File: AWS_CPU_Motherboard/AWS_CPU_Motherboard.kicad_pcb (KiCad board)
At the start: 4 copper layers, 255 x 305 mm, 53 parts, among them J1 Power, J10 UART B, J12 Video, J14 HDD Power, J15 HDD Power, J2 Speaker, J3 Cluster, J4 Cluster, J5 HDD Power, J6 Drive Type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

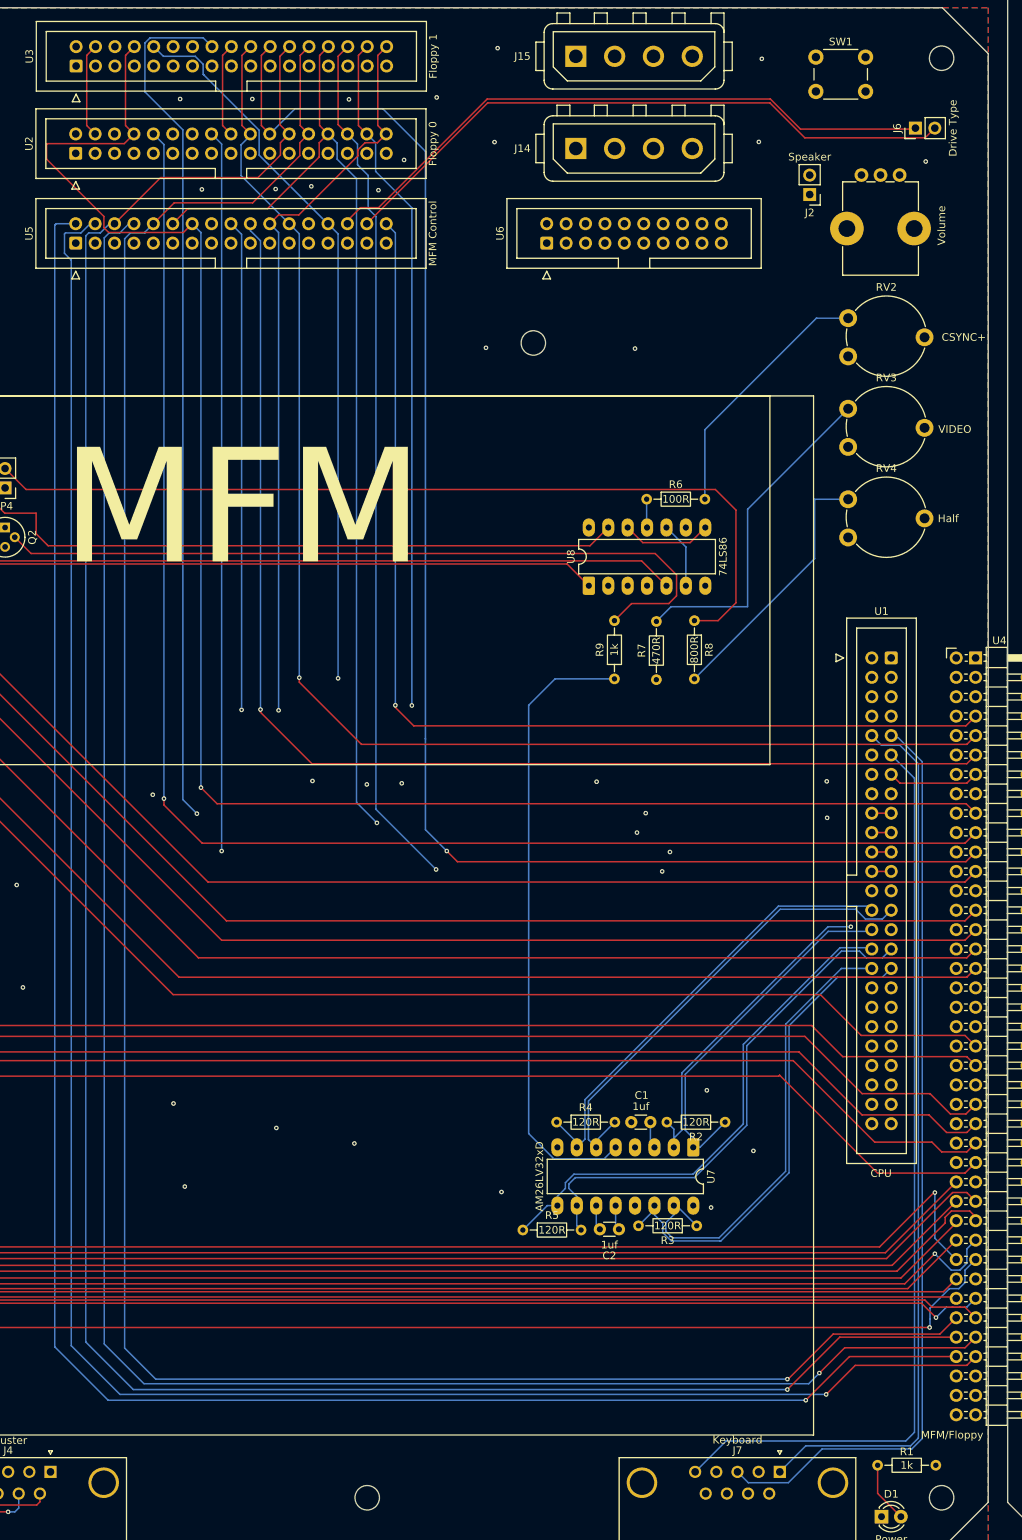
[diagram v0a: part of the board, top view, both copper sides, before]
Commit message: Update PCB to fix floppy drive & update video software to capure all the screen
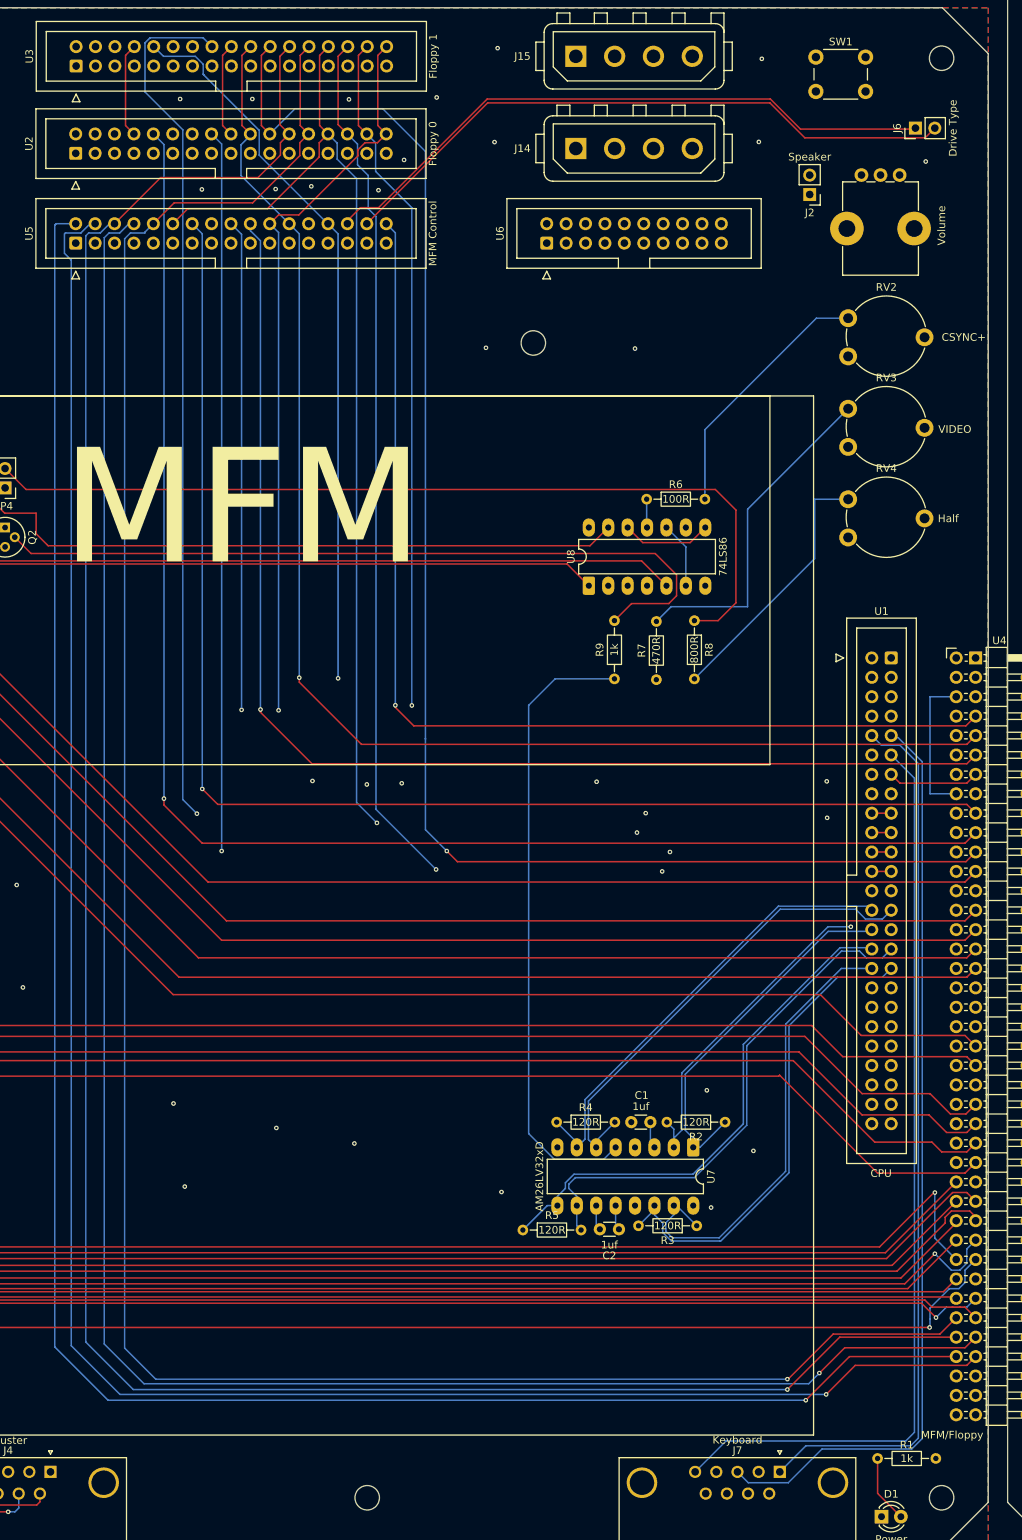
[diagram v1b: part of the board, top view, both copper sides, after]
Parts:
- moved R1 0.89 mm to (445.3, 450.2)
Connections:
- U2 pad 4: SIDED- -> unconnected-(U2-SIDED--Pad4)
- U2 pad 8: HDSEL0- -> INDEX-
- U3 pad 4: SIDED- -> unconnected-(U3-SIDED--Pad4)
- U3 pad 8: HDSEL0- -> INDEX-
- U4 pad 16: SIDED- -> 2SIDED-
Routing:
- net SIDED-: track 208.1 -> 0.00 mm, vias 1 -> 0
- net HDSEL0-: track 227.7 -> 177.1 mm
- net INDEX-: track 161.4 -> 196.0 mm
- net 2SIDED-: track 161.3 -> 180.9 mm
- net Net-(D1-A): track 7.99 -> 8.88 mm
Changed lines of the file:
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@@
 	(net 33 "WRDATA-")
 	(net 34 "RDDATA-")
-	(net 35 "SIDED-")
+	(net 35 "unconnected-(U2-SIDED--Pad4)")
 	(net 36 "WRGATE-")
 	(net 37 "unconnected-(U2-Pad12)")
@@
 	(net 173 "Net-(U8-Pad12)")
 	(net 174 "Net-(U8-Pad3)")
+	(net 175 "unconnected-(U3-SIDED--Pad4)")
 	(footprint "Connector_PinHeader_2.54mm:PinHeader_1x02_P2.54mm_Vertical"
 		(layer "F.Cu")
@@
 			(layers "*.Cu" "*.Mask")
 			(remove_unused_layers no)
-			(net 35 "SIDED-")
+			(net 32 "2SIDED-")
 			(pinfunction "SIDED-")
 			(pintype "bidirectional")
@@
 			(layers "*.Cu" "*.Mask")
 			(remove_unused_layers no)
-			(net 35 "SIDED-")
+			(net 175 "unconnected-(U3-SIDED--Pad4)")
 			(pinfunction "SIDED-")
-			(pintype "input")
+			(pintype "input+no_connect")
 		)
 		(pad "5" thru_hole circle
@@
 			(layers "*.Cu" "*.Mask")
 			(remove_unused_layers no)
-			(net 43 "HDSEL0-")
+			(net 71 "INDEX-")
 			(pinfunction "HDSEL0-")
 			(pintype "input")
@@
 			(layers "*.Cu" "*.Mask")
 			(remove_unused_layers no)
-			(net 35 "SIDED-")
+			(net 35 "unconnected-(U2-SIDED--Pad4)")
 			(pinfunction "SIDED-")
-			(pintype "input")
+			(pintype "input+no_connect")
 		)
 		(pad "5" thru_hole circle
@@
 			(layers "*.Cu" "*.Mask")
 			(remove_unused_layers no)
-			(net 43 "HDSEL0-")
+			(net 71 "INDEX-")
 			(pinfunction "HDSEL0-")
 			(pintype "input")
@@
 	(footprint "Resistor_THT:R_Axial_DIN0204_L3.6mm_D1.6mm_P7.62mm_Horizontal"
 		(layer "F.Cu")
-		(at 445.262 451.104 180)
+		(at 445.262 450.215 180)
 		(descr "Resistor, Axial_DIN0204 series, Axial, Horizontal, pin pitch=7.62mm, 0.167W, length*diameter=3.6*1.6mm^2, http://cdn-reichelt.de/documents/datenblatt/B400/1_4W%23YAG.pdf")
 		(tags "Resistor Axial_DIN0204 series Axial Horizontal pin pitch 7.62mm 0.167W length 3.6mm diameter 1.6mm")
@@
 	)
 	(segment
-		(start 437.642 451.104)
+		(start 437.642 450.215)
 		(end 437.642 454.787)
 		(width 0.2)
@@
 	)
 	(segment
+		(start 444.5 363.22)
+		(end 444.5 350.52)
+		(width 0.2)
+		(layer "B.Cu")
+		(net 32)
+	)
+	(segment
 		(start 371.9402 281.7702)
 		(end 371.9402 278.011)
@@
 	)
 	(segment
+		(start 444.5 350.52)
+		(end 447.929 350.52)
+		(width 0.2)
+		(layer "B.Cu")
+		(net 32)
+	)
+	(segment
+		(start 447.929 363.22)
+		(end 444.5 363.22)
+		(width 0.2)
+		(layer "B.Cu")
+		(net 32)
+	)
+	(segment
 		(start 387.85 351.671)
 		(end 446.778 351.671)
@@
 	)
 	(segment
-		(start 334.129 266.581)
-		(end 334.129 275.7598)
-		(width 0.2)
-		(layer "F.Cu")
-		(net 35)
-	)
-	(segment
-		(start 335.28 265.43)
-		(end 334.129 266.581)
-		(width 0.2)
-		(layer "F.Cu")
-		(net 35)
-	)
-	(segment
-		(start 334.129 275.7598)
-		(end 335.2292 276.86)
-		(width 0.2)
-		(layer "F.Cu")
-		(net 35)
-	)
-	(via
-		(at 342.773 363.347)
-		(size 0.6)
-		(drill 0.3)
-		(layers "F.Cu" "B.Cu")
-		(net 35)
-	)
-	(segment
-		(start 343.916 364.49)
-		(end 446.659 364.49)
-		(width 0.2)
-		(layer "In1.Cu")
-		(net 35)
-	)
-	(segment
-		(start 342.773 363.347)
-		(end 343.916 364.49)
-		(width 0.2)
-		(layer "In1.Cu")
-		(net 35)
-	)
-	(segment
-		(start 446.659 364.49)
-		(end 447.929 363.22)
-		(width 0.2)
-		(layer "In1.Cu")
-		(net 35)
-	)
-	(segment
-		(start 336.423 280.416)
-		(end 336.423 278.0538)
-		(width 0.2)
-		(layer "In2.Cu")
-		(net 35)
-	)
-	(segment
-		(start 336.423 278.0538)
-		(end 335.2292 276.86)
-		(width 0.2)
-		(layer "In2.Cu")
-		(net 35)
-	)
-	(segment
-		(start 341.63 362.204)
-		(end 341.63 285.623)
-		(width 0.2)
-		(layer "In2.Cu")
-		(net 35)
-	)
-	(segment
-		(start 341.63 285.623)
-		(end 336.423 280.416)
-		(width 0.2)
-		(layer "In2.Cu")
-		(net 35)
-	)
-	(segment
-		(start 342.773 363.347)
-		(end 341.63 362.204)
-		(width 0.2)
-		(layer "In2.Cu")
-		(net 35)
-	)
-	(segment
 		(start 432.689 434.34)
 		(end 447.929 434.34)
@@
 	)
 	(segment
-		(start 339.0392 278.13)
-		(end 340.3092 276.86)
-		(width 0.2)
-		(layer "F.Cu")
-		(net 43)
-	)
-	(segment
-		(start 328.8792 280.162)
-		(end 328.8792 278.2316)
-		(width 0.2)
-		(layer "F.Cu")
-		(net 43)
-	)
-	(segment
-		(start 339.209 266.581)
-		(end 339.209 275.7598)
-		(width 0.2)
-		(layer "F.Cu")
-		(net 43)
-	)
-	(segment
-		(start 347.9292 288.61)
-		(end 346.7782 289.761)
+		(start 349.25 362.585)
+		(end 351.274 364.609)
 		(width 0.2)
 		(layer "F.Cu")
@@
 	)
 	(segment
-		(start 349.0802 362.4152)
-		(end 351.189 364.524)
+		(start 351.274 364.609)
+		(end 449.318 364.609)
 		(width 0.2)
 		(layer "F.Cu")
@@
 	)
 	(segment
-		(start 449.233 364.524)
+		(start 449.318 364.609)
 		(end 450.469 365.76)
 		(width 0.2)
@@
 		(net 43)
 	)
-	(segment
-		(start 336.3802 289.1362)
-		(end 336.3802 287.663)
-		(width 0.2)
-		(layer "F.Cu")
-		(net 43)
-	)
-	(segment
-		(start 351.189 364.524)
-		(end 449.233 364.524)
-		(width 0.2)
-		(layer "F.Cu")
-		(net 43)
-	)
-	(segment
-		(start 346.7782 289.761)
-		(end 337.005 289.761)
-		(width 0.2)
-		(layer "F.Cu")
-		(net 43)
-	)
-	(segment
-		(start 328.8792 278.2316)
-		(end 328.9808 278.13)
-		(width 0.2)
-		(layer "F.Cu")
-		(net 43)
-	)
-	(segment
-		(start 336.3802 287.663)
-		(end 328.8792 280.162)
-		(width 0.2)
-		(layer "F.Cu")
-		(net 43)
-	)
-	(segment
-		(start 340.36 265.43)
-		(end 339.209 266.581)
-		(width 0.2)
-		(layer "F.Cu")
-		(net 43)
-	)
-	(segment
-		(start 328.9808 278.13)
-		(end 339.0392 278.13)
-		(width 0.2)
-		(layer "F.Cu")
-		(net 43)
-	)
-	(segment
-		(start 337.005 289.761)
-		(end 336.3802 289.1362)
-		(width 0.2)
-		(layer "F.Cu")
-		(net 43)
-	)
-	(segment
-		(start 339.209 275.7598)
-		(end 340.3092 276.86)
-		(width 0.2)
-		(layer "F.Cu")
-		(net 43)
-	)
 	(via
-		(at 349.0802 362.4152)
+		(at 349.25 362.585)
 		(size 0.6)
 		(drill 0.3)
@@
 	)
 	(segment
-		(start 349.0802 289.761)
-		(end 347.9292 288.61)
+		(start 349.25 289.9308)
+		(end 349.25 362.585)
 		(width 0.2)
 		(layer "B.Cu")
@@
 	)
 	(segment
-		(start 349.0802 362.4152)
-		(end 349.0802 289.761)
+		(start 347.9292 288.61)
+		(end 349.25 289.9308)
 		(width 0.2)
 		(layer "B.Cu")
@@
 	)
 	(segment
+		(start 340.36 265.43)
+		(end 339.209 266.581)
+		(width 0.2)
+		(layer "F.Cu")
+		(net 71)
+	)
+	(segment
+		(start 339.209 275.7598)
+		(end 340.3092 276.86)
+		(width 0.2)
+		(layer "F.Cu")
+		(net 71)
+	)
+	(segment
 		(start 363.609 359.291)
 		(end 449.318 359.291)
@@
 	)
 	(segment
+		(start 339.209 266.581)
+		(end 339.209 275.7598)
+		(width 0.2)
+		(layer "F.Cu")
+		(net 71)
+	)
+	(segment
 		(start 356.87 352.1964)
 		(end 356.87 352.552)
@@
 		(net 71)
 	)
+	(segment
+		(start 355.5492 288.61)
+		(end 348.8792 281.94)
+		(width 0.2)
+		(layer "In2.Cu")
+		(net 71)
+	)
+	(segment
+		(start 341.63 278.1808)
+		(end 340.3092 276.86)
+		(width 0.2)
+		(layer "In2.Cu")
+		(net 71)
+	)
+	(segment
+		(start 348.8792 281.94)
+		(end 341.63 281.94)
+		(width 0.2)
+		(layer "In2.Cu")
+		(net 71)
+	)
+	(segment
+		(start 341.63 281.94)
+		(end 341.63 278.1808)
+		(width 0.2)
+		(layer "In2.Cu")
+		(net 71)
+	)
